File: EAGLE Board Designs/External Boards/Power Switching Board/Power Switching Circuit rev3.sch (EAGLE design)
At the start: 65 parts, among them J1 CONNECTOR-3_, J2 CONNECTOR-4_SOURIAU_, J3 CONNECTOR-4_SOURIAU_, Q1 TRANSISTOR_N_MOS_2-7K1S_TK100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, Q2 TRANSISTOR_N_MOS_2-7K1S_TK100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, Q3 TRANSISTOR_N_MOS_2-7K1S_TK100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, Q4 TRANSISTOR_N_MOS_2-7K1S_TK100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, U1 LTC4421

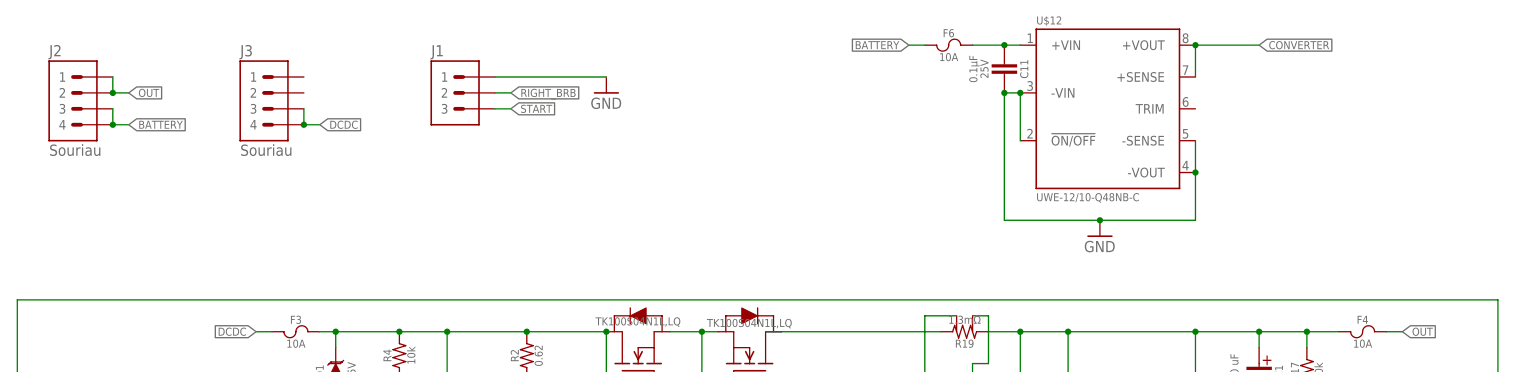
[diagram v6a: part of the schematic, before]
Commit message: Fixed buck converter capacitors
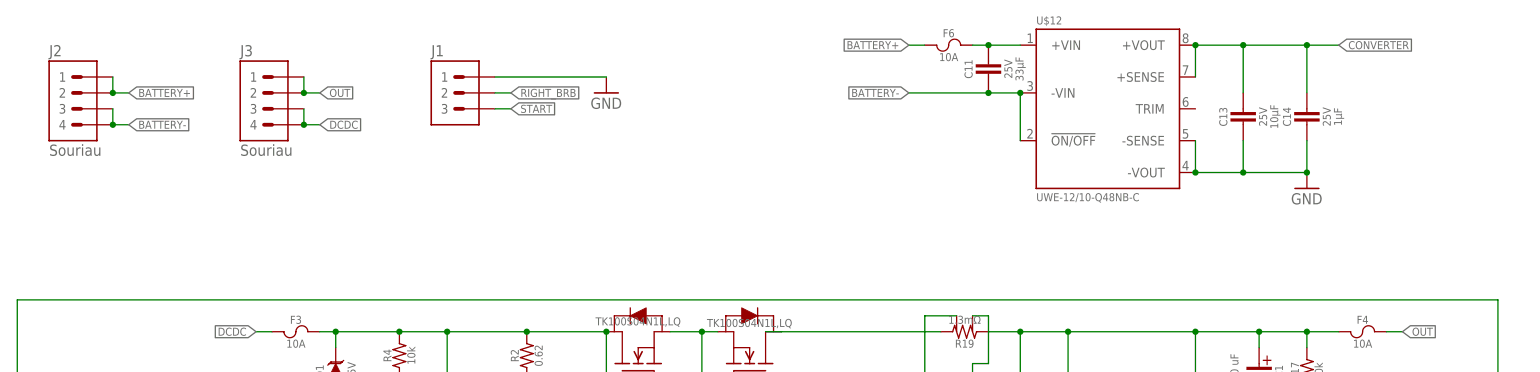
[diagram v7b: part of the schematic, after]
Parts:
- added C13: CAPACITOR_0603_25V_10UF, HyTechDevices:CAPACITOR_0603_25V_10UF
- added C14: CAPACITOR_0603_25V_1UF, HyTechDevices:CAPACITOR_0603_25V_1UF
- C11: value CAPACITOR_0603_25V_0.1UF -> CAPACITOR_1206_25V_33UF; device HyTechDevices:CAPACITOR_0603_25V_0.1UF -> HyTechDevices:CAPACITOR_1206_25V_33UF
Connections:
- removed net BATTERY: F6.1, J2.3, J2.4
- new net BATTERY+: F6.1, J2.1, J2.2
- new net BATTERY-: C11.2, J2.3, J2.4, U$12.!ON/OFF, U$12.-VIN
- net CONVERTER: now also C13.1, C14.1
- net GND: now also C13.2, C14.2; no longer C11.1, U$12.!ON/OFF, U$12.-VIN
- net N$29: now also C11.1; no longer C11.2
- net OUT: now also J3.1, J3.2; no longer J2.1, J2.2
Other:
- moved on the sheet: C11
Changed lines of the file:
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@@
 <part name="F6" library="HyTechDevices" deviceset="FUSE_?_*" device="MB" technology="10" value="FUSE_MB_10"/>
 <part name="GND15" library="HyTechSupplies" deviceset="GND" device=""/>
-<part name="C11" library="HyTechDevices" deviceset="CAPACITOR_?_*" device="0603" technology="25V_0.1UF"/>
 <part name="R2" library="HyTechDevices" deviceset="RESISTOR_?_*" device="0805" technology="0.62"/>
 <part name="R12" library="HyTechDevices" deviceset="RESISTOR_?_*" device="0805" technology="0.62"/>
+<part name="C13" library="HyTechDevices" deviceset="CAPACITOR_?_*" device="0603" technology="25V_10UF"/>
+<part name="C14" library="HyTechDevices" deviceset="CAPACITOR_?_*" device="0603" technology="25V_1UF"/>
+<part name="C11" library="HyTechDevices" deviceset="CAPACITOR_?_*" device="1206" technology="25V_33UF"/>
 </parts>
 <sheets>
@@
 <attribute name="CURRENT" x="34.29" y="90.17" size="1.27" layer="96" align="top-center"/>
 </instance>
-<instance part="GND15" gate="1" x="58.42" y="60.96" smashed="yes">
-<attribute name="VALUE" x="55.88" y="58.42" size="1.778" layer="96"/>
-</instance>
-<instance part="C11" gate="G$1" x="43.18" y="86.36" smashed="yes" rot="R270">
-<attribute name="NAME" x="45.72" y="87.63" size="1.27" layer="95" rot="R270" align="bottom-center"/>
-<attribute name="VOLTAGE" x="40.64" y="87.63" size="1.27" layer="96" rot="R270" align="top-center"/>
-<attribute name="CAPACITANCE" x="38.862" y="87.63" size="1.27" layer="96" rot="R270" align="top-center"/>
+<instance part="GND15" gate="1" x="91.44" y="68.58" smashed="yes">
+<attribute name="VALUE" x="88.9" y="66.04" size="1.778" layer="96"/>
 </instance>
 <instance part="R2" gate="G$1" x="-33.02" y="43.18" smashed="yes" rot="R90">
@@
 <attribute name="NAME" x="-41.91" y="21.59" size="1.27" layer="95" rot="R90" align="bottom-center"/>
 <attribute name="RESISTANCE" x="-39.37" y="21.59" size="1.27" layer="96" rot="R90" align="top-center"/>
+</instance>
+<instance part="C13" gate="G$1" x="81.28" y="81.28" smashed="yes" rot="R90">
+<attribute name="NAME" x="78.74" y="80.01" size="1.27" layer="95" rot="R90" align="bottom-center"/>
+<attribute name="VOLTAGE" x="83.82" y="80.01" size="1.27" layer="96" rot="R90" align="top-center"/>
+<attribute name="CAPACITANCE" x="85.598" y="80.01" size="1.27" layer="96" rot="R90" align="top-center"/>
+</instance>
+<instance part="C14" gate="G$1" x="91.44" y="81.28" smashed="yes" rot="R90">
+<attribute name="NAME" x="88.9" y="80.01" size="1.27" layer="95" rot="R90" align="bottom-center"/>
+<attribute name="VOLTAGE" x="93.98" y="80.01" size="1.27" layer="96" rot="R90" align="top-center"/>
+<attribute name="CAPACITANCE" x="95.758" y="80.01" size="1.27" layer="96" rot="R90" align="top-center"/>
+</instance>
+<instance part="C11" gate="G$1" x="40.64" y="88.9" smashed="yes" rot="R90">
+<attribute name="NAME" x="38.1" y="87.63" size="1.27" layer="95" rot="R90" align="bottom-center"/>
+<attribute name="VOLTAGE" x="43.18" y="87.63" size="1.27" layer="96" rot="R90" align="top-center"/>
+<attribute name="CAPACITANCE" x="44.958" y="87.63" size="1.27" layer="96" rot="R90" align="top-center"/>
 </instance>
 </instances>
@@
 </segment>
 <segment>
-<pinref part="U$12" gate="G$1" pin="-VIN"/>
-<pinref part="U$12" gate="G$1" pin="!ON/OFF"/>
-<wire x1="45.72" y1="76.2" x2="45.72" y2="83.82" width="0.1524" layer="91"/>
-<junction x="45.72" y="83.82"/>
-<wire x1="45.72" y1="83.82" x2="43.18" y2="83.82" width="0.1524" layer="91"/>
-<pinref part="C11" gate="G$1" pin="1"/>
+<pinref part="U$12" gate="G$1" pin="-SENSE"/>
+<pinref part="U$12" gate="G$1" pin="-VOUT"/>
+<wire x1="73.66" y1="71.12" x2="73.66" y2="76.2" width="0.1524" layer="91"/>
 <pinref part="GND15" gate="1" pin="GND"/>
-<wire x1="43.18" y1="83.82" x2="43.18" y2="63.5" width="0.1524" layer="91"/>
-<wire x1="43.18" y1="63.5" x2="58.42" y2="63.5" width="0.1524" layer="91"/>
-<junction x="43.18" y="83.82"/>
-<pinref part="U$12" gate="G$1" pin="-VOUT"/>
-<pinref part="U$12" gate="G$1" pin="-SENSE"/>
-<wire x1="73.66" y1="71.12" x2="73.66" y2="76.2" width="0.1524" layer="91"/>
-<wire x1="58.42" y1="63.5" x2="73.66" y2="63.5" width="0.1524" layer="91"/>
-<wire x1="73.66" y1="63.5" x2="73.66" y2="71.12" width="0.1524" layer="91"/>
-<junction x="58.42" y="63.5"/>
+<wire x1="91.44" y1="71.12" x2="81.28" y2="71.12" width="0.1524" layer="91"/>
 <junction x="73.66" y="71.12"/>
-</segment>
-</net>
-<net name="BATTERY" class="0">
-<segment>
-<wire x1="-99.06" y1="78.74" x2="-96.52" y2="78.74" width="0.1524" layer="91"/>
-<label x="-96.52" y="78.74" size="1.27" layer="95" xref="yes"/>
-<pinref part="J2" gate="G$1" pin="4"/>
-<pinref part="J2" gate="G$1" pin="3"/>
-<wire x1="-99.06" y1="81.28" x2="-99.06" y2="78.74" width="0.1524" layer="91"/>
-<junction x="-99.06" y="78.74"/>
-</segment>
-<segment>
-<pinref part="F6" gate="G$1" pin="1"/>
-<wire x1="30.48" y1="91.44" x2="27.94" y2="91.44" width="0.1524" layer="91"/>
-<label x="27.94" y="91.44" size="1.27" layer="95" rot="R180" xref="yes"/>
+<pinref part="C14" gate="G$1" pin="2"/>
+<wire x1="81.28" y1="71.12" x2="73.66" y2="71.12" width="0.1524" layer="91"/>
+<wire x1="91.44" y1="71.12" x2="91.44" y2="76.2" width="0.1524" layer="91"/>
+<junction x="91.44" y="71.12"/>
+<pinref part="C13" gate="G$1" pin="2"/>
+<wire x1="81.28" y1="76.2" x2="81.28" y2="71.12" width="0.1524" layer="91"/>
+<junction x="81.28" y="71.12"/>
 </segment>
 </net>
@@
 </segment>
 <segment>
-<wire x1="-99.06" y1="83.82" x2="-96.52" y2="83.82" width="0.1524" layer="91"/>
-<label x="-96.52" y="83.82" size="1.27" layer="95" xref="yes"/>
-<pinref part="J2" gate="G$1" pin="2"/>
-<pinref part="J2" gate="G$1" pin="1"/>
-<wire x1="-99.06" y1="83.82" x2="-99.06" y2="86.36" width="0.1524" layer="91"/>
-<junction x="-99.06" y="83.82"/>
-</segment>
-<segment>
 <pinref part="F4" gate="G$1" pin="2"/>
 <wire x1="104.14" y1="45.72" x2="106.68" y2="45.72" width="0.1524" layer="91"/>
 <label x="106.68" y="45.72" size="1.27" layer="95" xref="yes"/>
+</segment>
+<segment>
+<pinref part="J3" gate="G$1" pin="2"/>
+<pinref part="J3" gate="G$1" pin="1"/>
+<wire x1="-68.58" y1="83.82" x2="-68.58" y2="86.36" width="0.1524" layer="91"/>
+<wire x1="-68.58" y1="83.82" x2="-66.04" y2="83.82" width="0.1524" layer="91"/>
+<junction x="-68.58" y="83.82"/>
+<label x="-66.04" y="83.82" size="1.27" layer="95" xref="yes"/>
 </segment>
 </net>
@@
 <segment>
 <pinref part="U$12" gate="G$1" pin="+VIN"/>
-<wire x1="45.72" y1="91.44" x2="43.18" y2="91.44" width="0.1524" layer="91"/>
 <pinref part="F6" gate="G$1" pin="2"/>
-<pinref part="C11" gate="G$1" pin="2"/>
-<wire x1="43.18" y1="91.44" x2="38.1" y2="91.44" width="0.1524" layer="91"/>
-<junction x="43.18" y="91.44"/>
+<wire x1="45.72" y1="91.44" x2="40.64" y2="91.44" width="0.1524" layer="91"/>
+<pinref part="C11" gate="G$1" pin="1"/>
+<wire x1="40.64" y1="91.44" x2="38.1" y2="91.44" width="0.1524" layer="91"/>
+<junction x="40.64" y="91.44"/>
 </segment>
 </net>
@@
 <segment>
 <pinref part="U$12" gate="G$1" pin="+VOUT"/>
-<wire x1="73.66" y1="91.44" x2="83.82" y2="91.44" width="0.1524" layer="91"/>
-<label x="83.82" y="91.44" size="1.27" layer="95" xref="yes"/>
+<label x="96.52" y="91.44" size="1.27" layer="95" xref="yes"/>
 <pinref part="U$12" gate="G$1" pin="+SENSE"/>
 <wire x1="73.66" y1="86.36" x2="73.66" y2="91.44" width="0.1524" layer="91"/>
 <junction x="73.66" y="91.44"/>
+<wire x1="73.66" y1="91.44" x2="81.28" y2="91.44" width="0.1524" layer="91"/>
+<pinref part="C13" gate="G$1" pin="1"/>
+<wire x1="81.28" y1="91.44" x2="91.44" y2="91.44" width="0.1524" layer="91"/>
+<wire x1="91.44" y1="91.44" x2="96.52" y2="91.44" width="0.1524" layer="91"/>
+<wire x1="81.28" y1="83.82" x2="81.28" y2="91.44" width="0.1524" layer="91"/>
+<junction x="81.28" y="91.44"/>
+<pinref part="C14" gate="G$1" pin="1"/>
+<wire x1="91.44" y1="83.82" x2="91.44" y2="91.44" width="0.1524" layer="91"/>
+<junction x="91.44" y="91.44"/>
 </segment>
 <segment>
@@
 </segment>
 </net>
+<net name="BATTERY+" class="0">
+<segment>
+<pinref part="J2" gate="G$1" pin="1"/>
+<pinref part="J2" gate="G$1" pin="2"/>
+<wire x1="-99.06" y1="86.36" x2="-99.06" y2="83.82" width="0.1524" layer="91"/>
+<wire x1="-99.06" y1="83.82" x2="-96.52" y2="83.82" width="0.1524" layer="91"/>
+<junction x="-99.06" y="83.82"/>
+<label x="-96.52" y="83.82" size="1.27" layer="95" xref="yes"/>
+</segment>
+<segment>
+<pinref part="F6" gate="G$1" pin="1"/>
+<wire x1="30.48" y1="91.44" x2="27.94" y2="91.44" width="0.1524" layer="91"/>
+<label x="27.94" y="91.44" size="1.27" layer="95" rot="R180" xref="yes"/>
+</segment>
+</net>
+<net name="BATTERY-" class="0">
+<segment>
+<wire x1="-99.06" y1="78.74" x2="-96.52" y2="78.74" width="0.1524" layer="91"/>
+<pinref part="J2" gate="G$1" pin="4"/>
+<pinref part="J2" gate="G$1" pin="3"/>
+<wire x1="-99.06" y1="81.28" x2="-99.06" y2="78.74" width="0.1524" layer="91"/>
+<junction x="-99.06" y="78.74"/>
+<label x="-96.52" y="78.74" size="1.27" layer="95" xref="yes"/>
+</segment>
+<segment>
+<pinref part="U$12" gate="G$1" pin="-VIN"/>
+<pinref part="U$12" gate="G$1" pin="!ON/OFF"/>
+<wire x1="45.72" y1="76.2" x2="45.72" y2="83.82" width="0.1524" layer="91"/>
+<junction x="45.72" y="83.82"/>
+<wire x1="45.72" y1="83.82" x2="40.64" y2="83.82" width="0.1524" layer="91"/>
+<label x="27.94" y="83.82" size="1.27" layer="95" rot="R180" xref="yes"/>
+<pinref part="C11" gate="G$1" pin="2"/>
+<wire x1="40.64" y1="83.82" x2="27.94" y2="83.82" width="0.1524" layer="91"/>
+<junction x="40.64" y="83.82"/>
+</segment>
+</net>

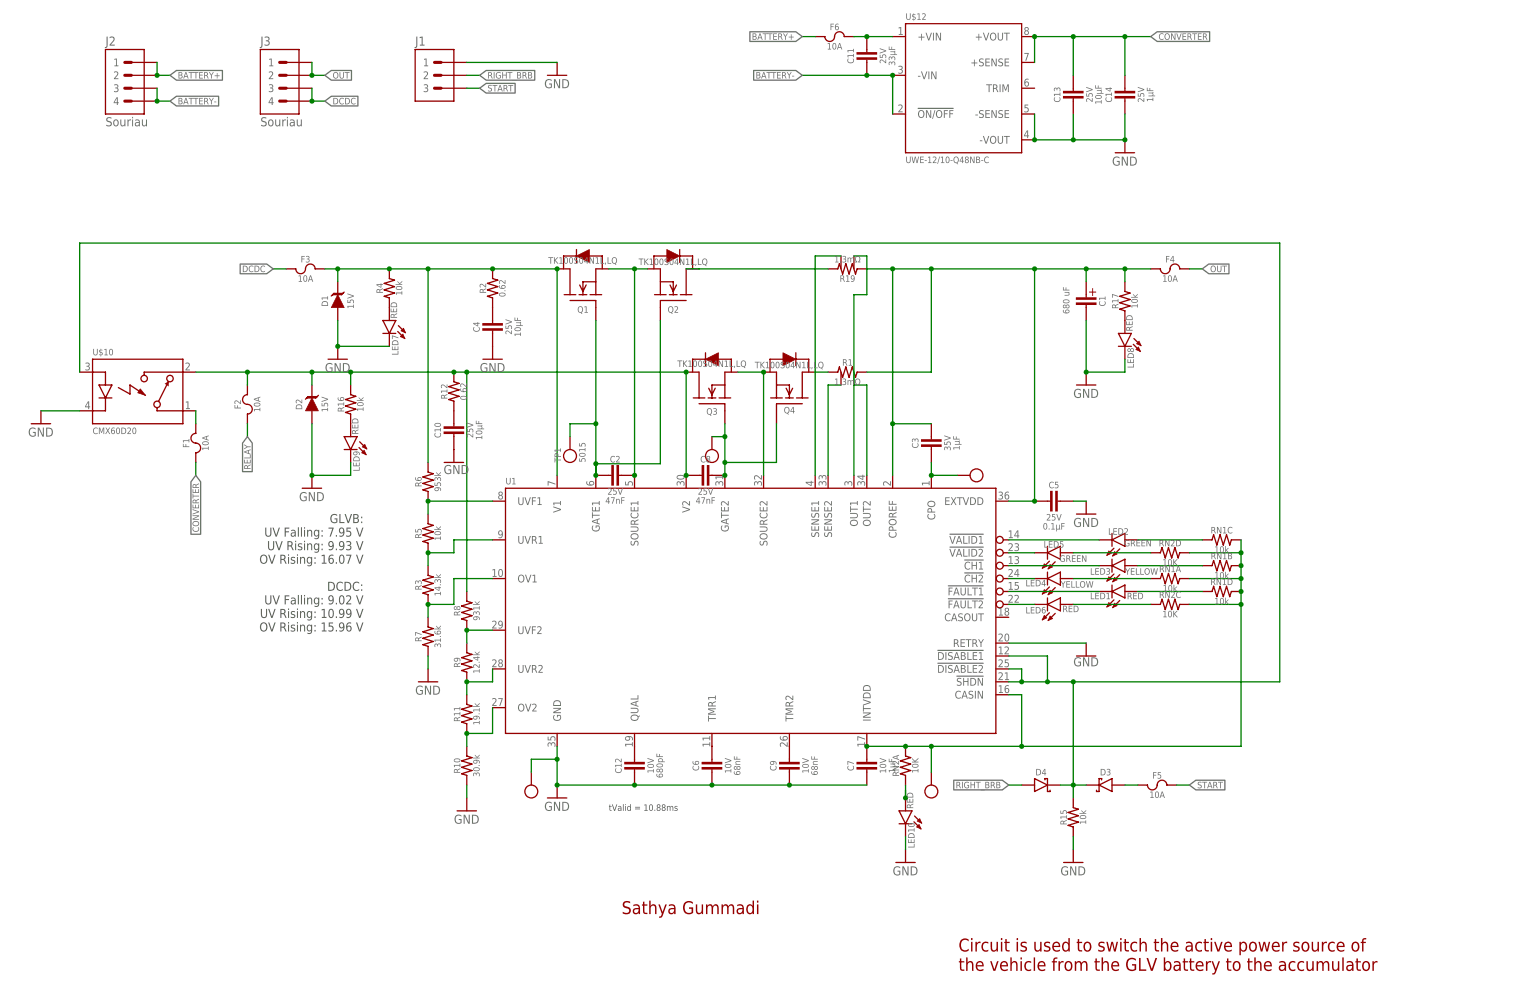
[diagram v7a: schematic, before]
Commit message: Replaced 10k resistors with ones in library
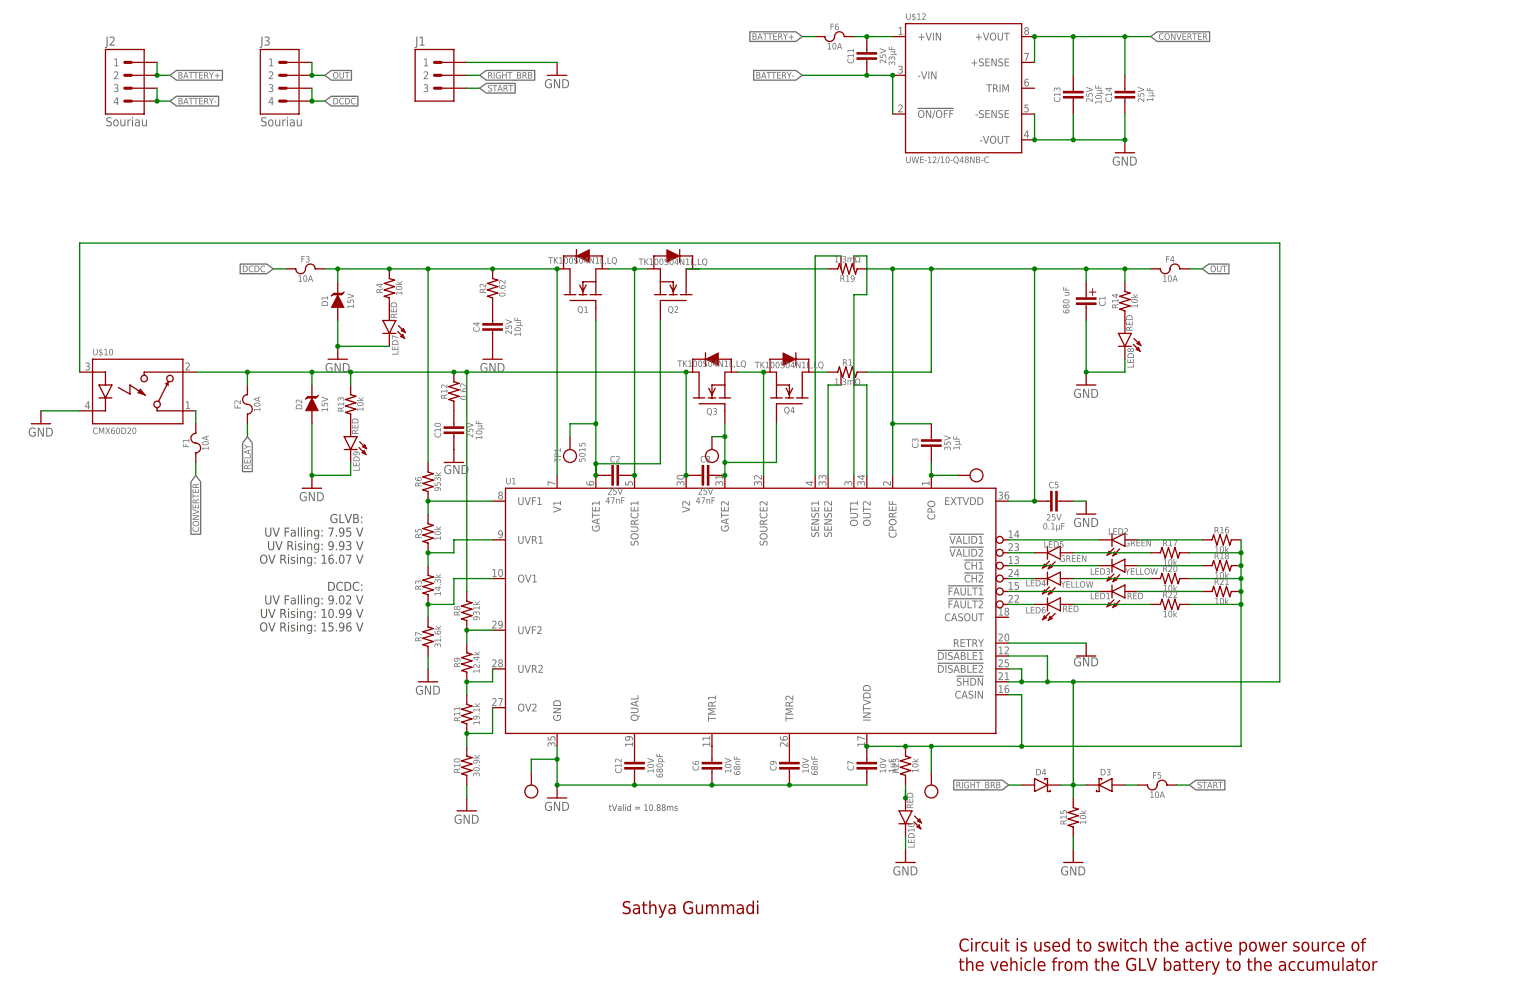
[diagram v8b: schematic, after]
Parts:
- removed RN1: RESISTOR_NETWORK_4_10K, HyTechDevices - Copy:RESISTOR_NETWORK_4_10K
- removed RN2: RESISTOR_NETWORK_4_10K, HyTechDevices:RESISTOR_NETWORK_4_10K
- added R13, R14, R18, R20, R21, R22, R23: RESISTOR_0603_10K, HyTechDevices:RESISTOR_0603_10K
- R15, R16, R17, R4: value 10k -> RESISTOR_0603_10K; device HyTechDevices:RESISTOR0603 -> HyTechDevices:RESISTOR_0603_10K
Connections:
- net N$10: now also R14.1; no longer R17.1
- net N$11: now also R22.1; no longer RN2C.1
- net N$13: now also R21.1; no longer RN1D.1
- net N$15: now also R20.1; no longer RN1A.1
- net N$17: now also R18.1; no longer RN1B.1
- net N$19: now also R17.1; no longer RN2D.1
- net N$21: now also R16.1; no longer RN1C.1
- net N$30: now also R16.2, R17.2, R18.2, R20.2, R21.2, R22.2, R23.2; no longer RN1A.2, RN1B.2, RN1C.2, RN1D.2, RN2A.2, RN2C.2, RN2D.2
- net N$6: now also R13.1; no longer R16.1
- net N$9: now also R23.1; no longer RN2A.1
- net OUT: now also R14.2; no longer R17.2
- net RELAY: now also R13.2; no longer R16.2
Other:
- moved on the sheet: R16, R17
